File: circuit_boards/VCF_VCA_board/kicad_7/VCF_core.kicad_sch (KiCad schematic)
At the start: 31 parts, among them U1 TL072, U2 TL072, U3 TL072, U8 SSI2140

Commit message: Progress on circuit boards
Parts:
- R207: value 56k -> 51k
- RV?: value ? -> 5k
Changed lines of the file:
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@@
   (title_block
     (title "MICRO-OX VCF/VCA board")
-    (date "2023-03-21")
+    (date "2023-04-13")
     (rev "0")
     (comment 1 "creativecommons.org/licenses/by/4.0/")
@@
       (effects (font (size 1.27 1.27)))
     )
-    (property "Value" "56k" (at 130.81 144.78 90)
+    (property "Value" "51k" (at 130.81 144.78 90)
       (effects (font (size 1.27 1.27)))
     )
@@
       (effects (font (size 1.27 1.27)))
     )
-    (property "Value" "?" (at 119.38 153.67 90)
-      (effects (font (size 1.27 1.27)))
-    )
+    (property "Value" "5k" (at 119.38 153.67 90)
+      (effects (font (size 1.27 1.27)))
+    )

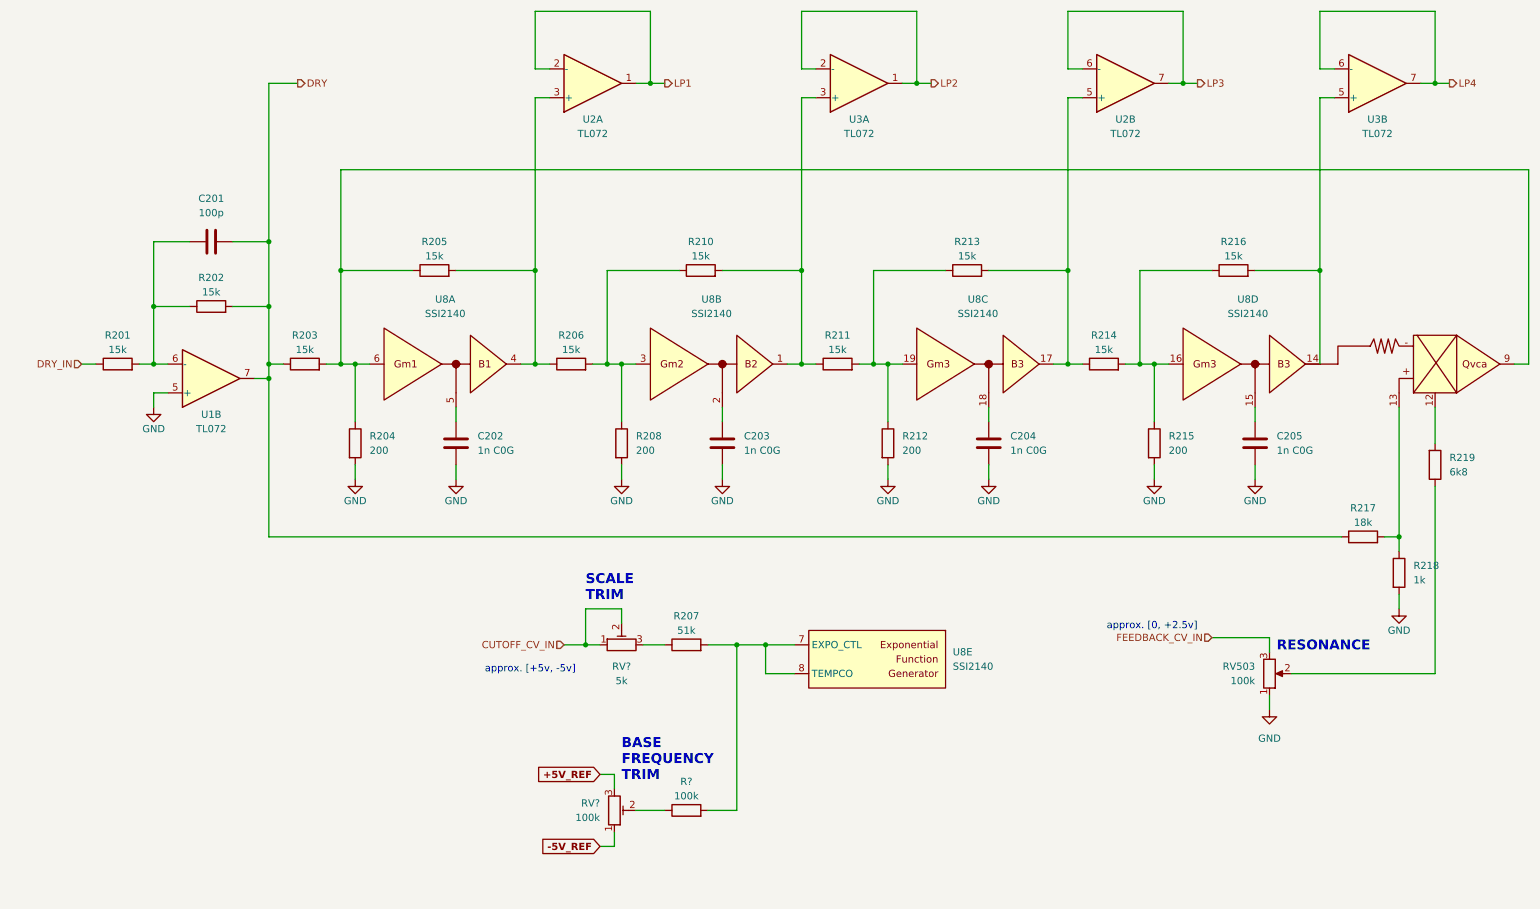
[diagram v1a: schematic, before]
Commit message: Update PCBs, tweak vals, add VCF CV from DAC
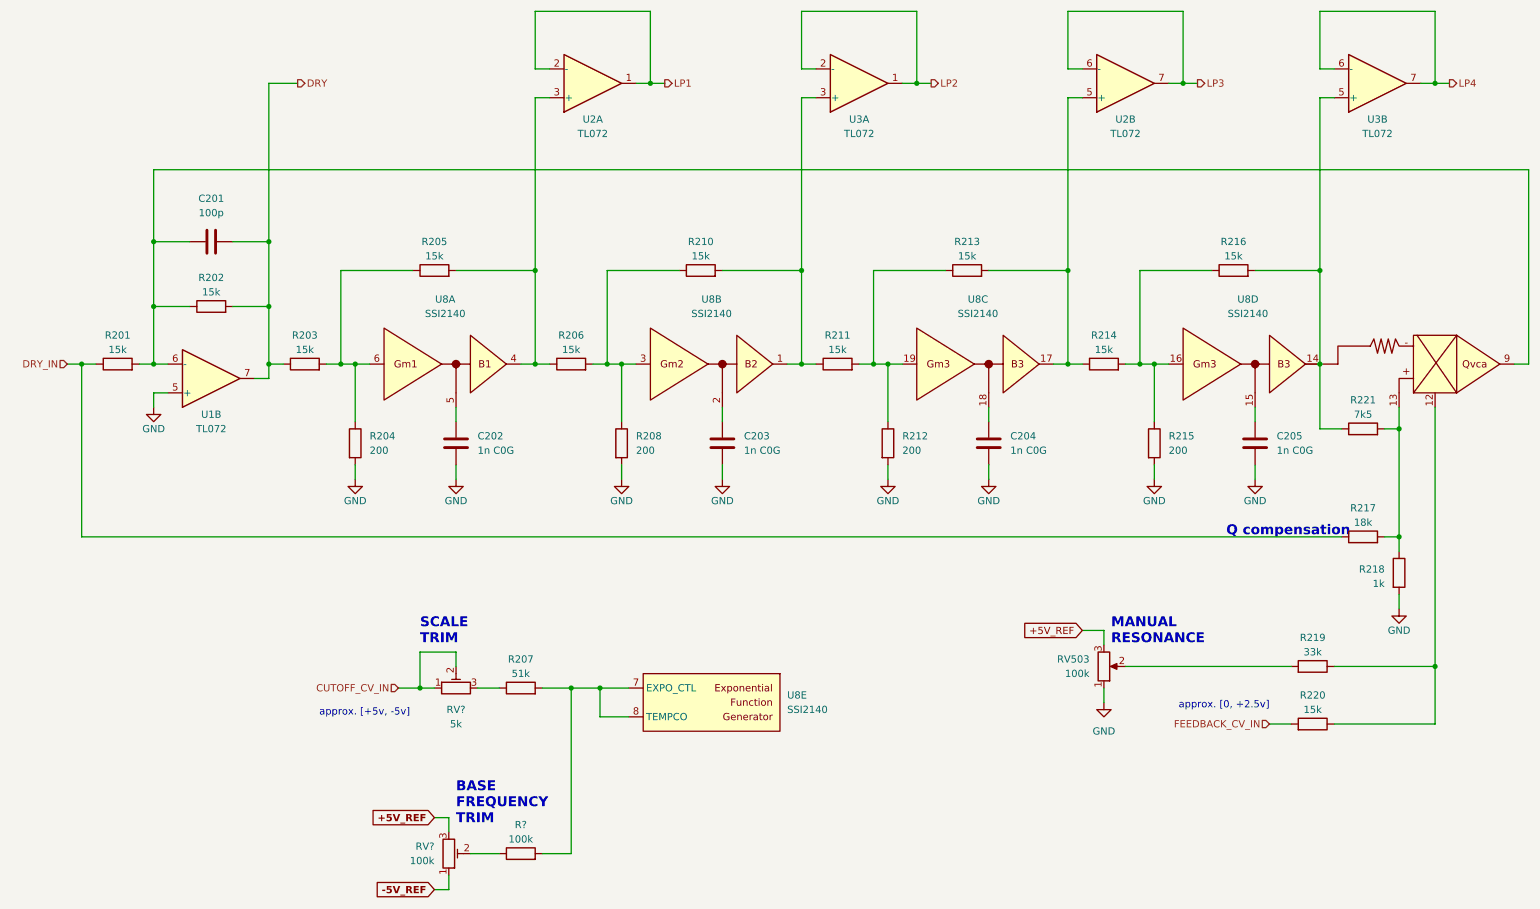
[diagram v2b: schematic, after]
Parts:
- added R220: 15k, Resistor_SMD:R_0603_1608Metric, symbol Device:R
- added R221: 7k5, Resistor_SMD:R_0603_1608Metric, symbol Device:R
- R219: value 6k8 -> 33k
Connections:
- net +5V_REF: now also RV503.3
- net DRY: no longer R217.1
- net DRY_IN: now also R217.1
- net FEEDBACK_CV_IN: now also R220.2; no longer RV503.3
- net at R216.2, U3.5 (+), U8.14: now also R221.1
- net at RV503.2: now also R219.2; no longer R219.1
- net at C201.1, R201.2, R202.1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: now also U8.9
- net at R203.2, R204.1, R205.1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: no longer U8.9
- net at R217.2, R218.1, U8.13: now also R221.2
- net at U8.12: now also R219.1, R220.1; no longer R219.2
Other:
- note added: "MANUAL RESONANCE"
- note added: "Q compensation"
- note removed: "RESONANCE"
- moved on the sheet: R207, R219, R?, RV503, RV?, U8E

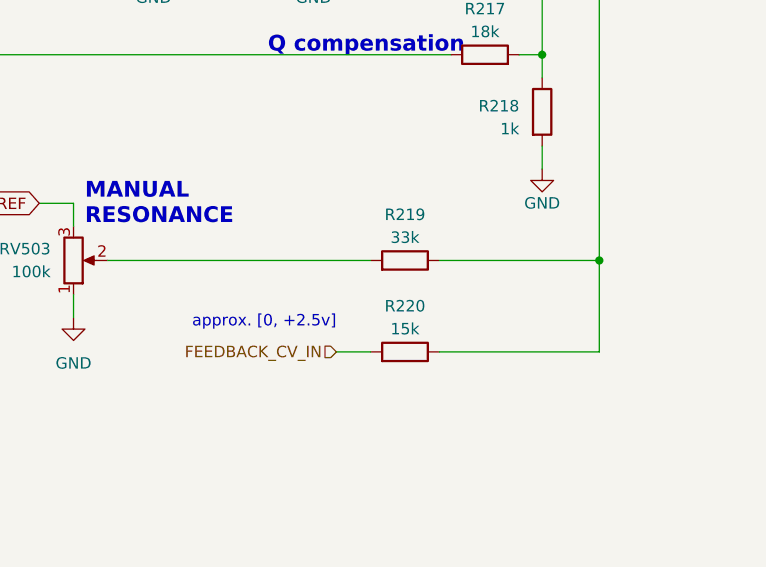
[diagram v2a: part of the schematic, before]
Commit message: Resistor tweaks while evaluating 1st build
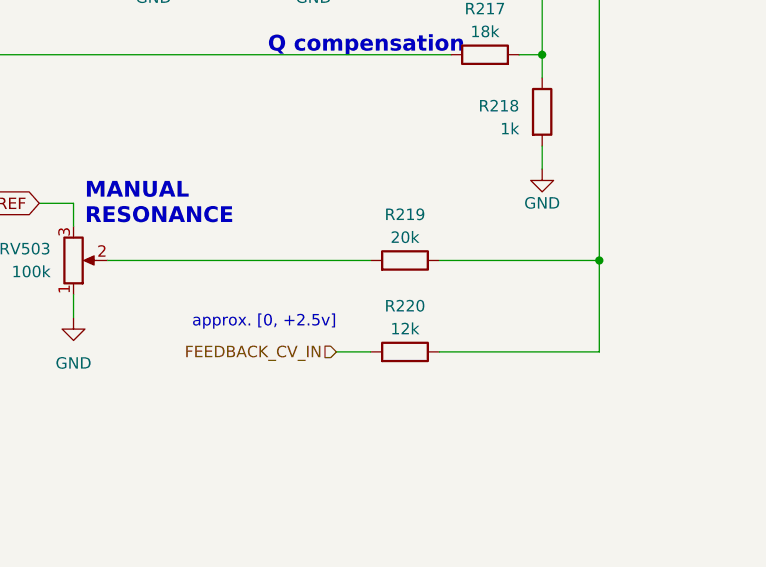
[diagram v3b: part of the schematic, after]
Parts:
- R219: value 33k -> 20k
- R220: value 15k -> 12k
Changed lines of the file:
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@@
       (effects (font (size 1.27 1.27)))
     )
-    (property "Value" "15k" (at 241.3 158.75 90)
+    (property "Value" "12k" (at 241.3 158.75 90)
       (effects (font (size 1.27 1.27)))
     )
@@
       (effects (font (size 1.27 1.27)))
     )
-    (property "Value" "33k" (at 241.3 148.59 90)
-      (effects (font (size 1.27 1.27)))
-    )
+    (property "Value" "20k" (at 241.3 148.59 90)
+      (effects (font (size 1.27 1.27)))
+    )

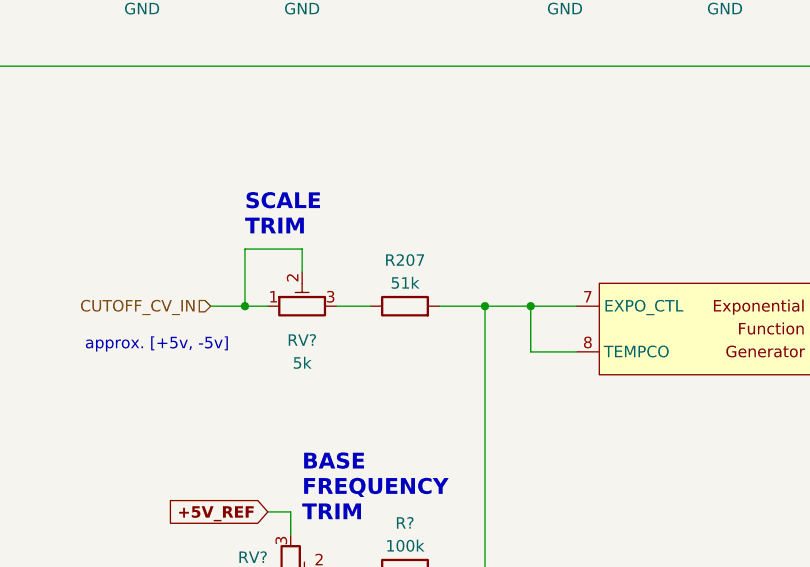
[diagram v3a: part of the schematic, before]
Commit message: Increase VCF 1v/oct drive so it can be trimmed to play in tune
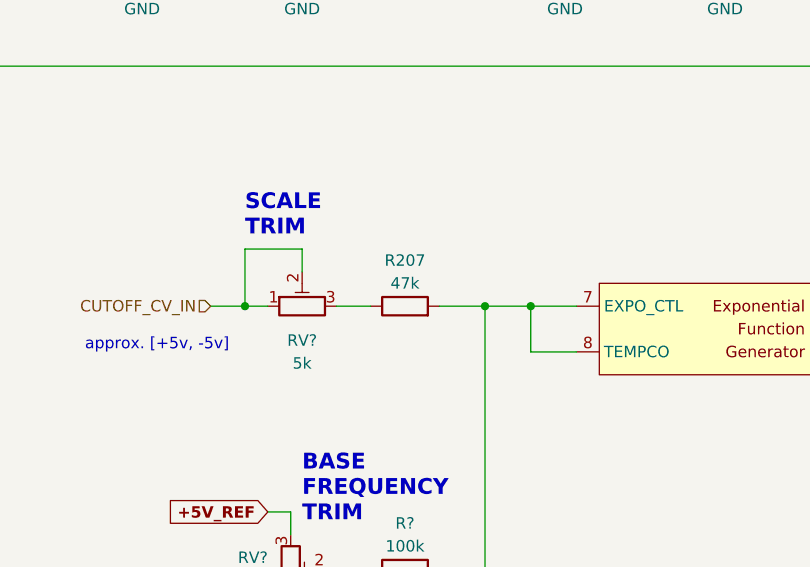
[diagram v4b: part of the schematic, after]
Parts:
- R207: value 51k -> 47k
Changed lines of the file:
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@@
       (effects (font (size 1.27 1.27)))
     )
-    (property "Value" "51k" (at 101.6 152.4 90)
+    (property "Value" "47k" (at 101.6 152.4 90)
       (effects (font (size 1.27 1.27)))
     )

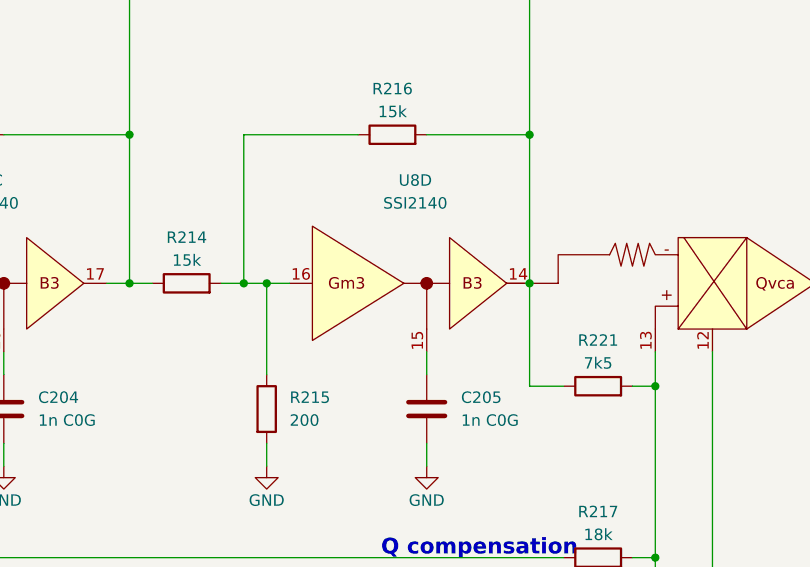
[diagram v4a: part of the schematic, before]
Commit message: Fix copy paste error with SSI2140 symbol, add potentiometer 3d model
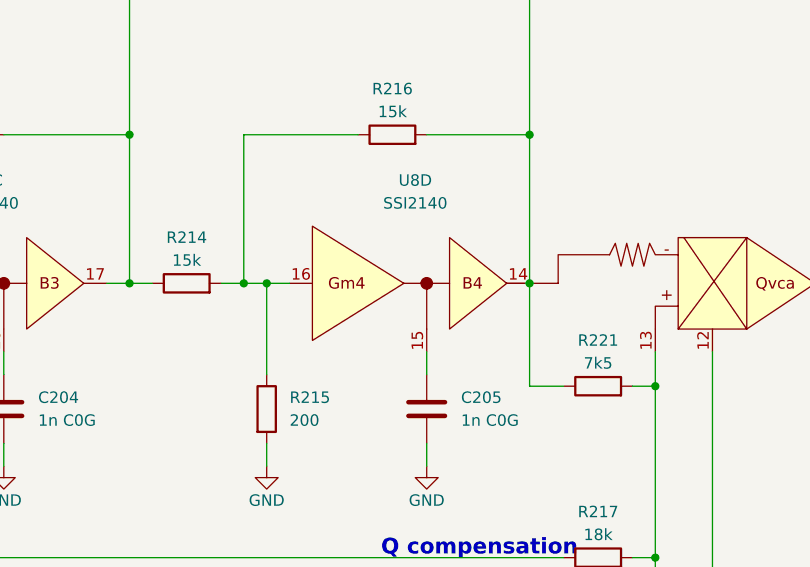
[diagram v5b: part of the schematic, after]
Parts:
- RV503: footprint Potentiometer_THT:Potentiometer_Alpha_RD901F-40-00D_Single_Vertical -> custom_footprints:Potentiometer_Alpha_RD901F-40-00D_Single_Vertical
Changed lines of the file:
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@@
       (effects (font (size 1.27 1.27)) (justify right))
     )
-    (property "Footprint" "Potentiometer_THT:Potentiometer_Alpha_RD901F-40-00D_Single_Vertical" (at 204.47 151.13 0)
+    (property "Footprint" "custom_footprints:Potentiometer_Alpha_RD901F-40-00D_Single_Vertical" (at 204.47 151.13 0)
       (effects (font (size 1.27 1.27)) hide)
     )

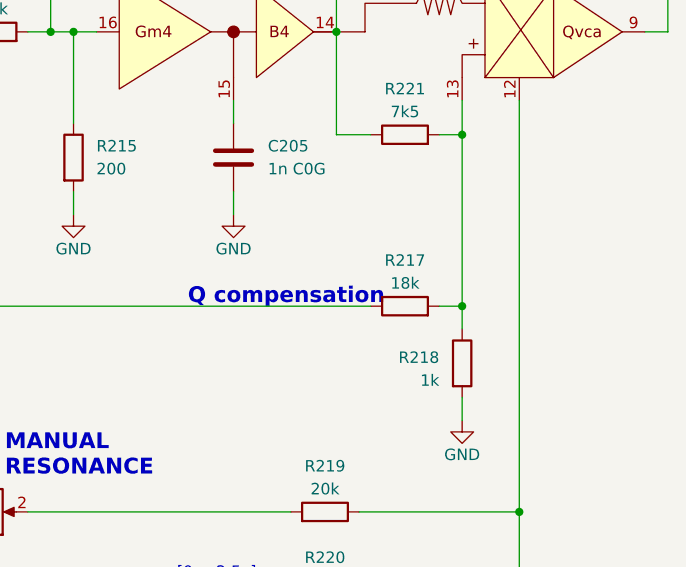
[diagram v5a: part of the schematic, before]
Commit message: Tone down Q-compensation to avoid volume increase with high Q
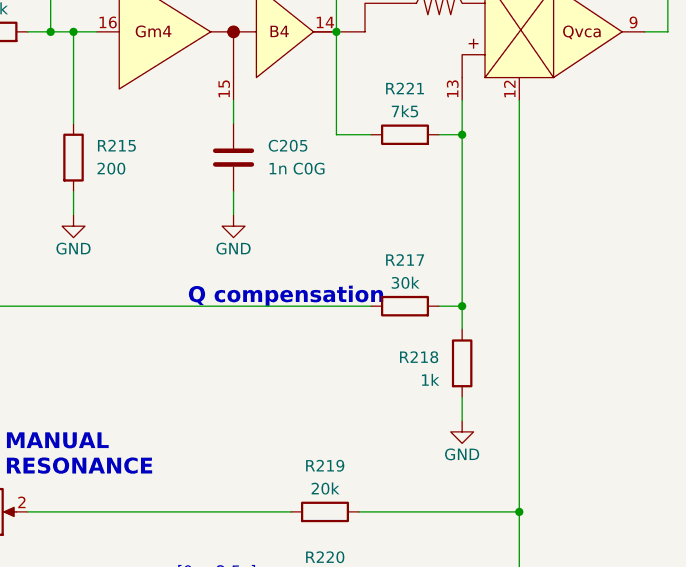
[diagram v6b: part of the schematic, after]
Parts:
- R217: value 18k -> 30k
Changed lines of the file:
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@@
       (effects (font (size 1.27 1.27)))
     )
-    (property "Value" "18k" (at 250.19 125.73 90)
+    (property "Value" "30k" (at 250.19 125.73 90)
       (effects (font (size 1.27 1.27)))
     )
